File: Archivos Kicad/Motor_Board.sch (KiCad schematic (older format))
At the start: 56 parts, among them IC1 L298, P1 CONN_2_V, P2 CONN_2_V, P3 CONN_2_V, SW1 SWITCH_INV, U1 74HC04, U2 7805

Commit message: Modificaciones: Se eliminaron los HC04 y se habilitaron directamente las entradas (IN1, IN2, IN3, IN4). Las salidas de los motores se conectaron directamente al L298.
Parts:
- removed U1: 74HC04, symbol 74HC04
- added D20, D21: Led_Small, symbol Led_Small
- added OK5, OK6: 4N35, DIL06, symbol 4N35
- added R16, R17: 330, symbol R
- added R18, R19: 1K, symbol R
- R11, R13, R14: value R -> 1K; Digikey# (none) -> Value; LibPart (none) -> Value; Manf (none) -> Value; Manf# (none) -> Value
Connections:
- net labels added: GPIO3, GPIO5
- wire segments 181 -> 199
- no-connect marks 29 -> 25
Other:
- moved on the sheet: D10, D11, D12, D13, D14, D15, D16, D17, D18, D5, D6, D9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

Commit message: Modificaciones en la asignación de tierras entre los optoacopladores y el conector de la Edu Ciaa. Nueva conexión de la tierra del led D19.
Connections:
- net labels removed: GND
- wire segments 199 -> 191
- no-connect marks 25 -> 34
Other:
- moved on the sheet: D1, D10, D11, D12, D13, D14, D15, D16, D17, D18, D2, D20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

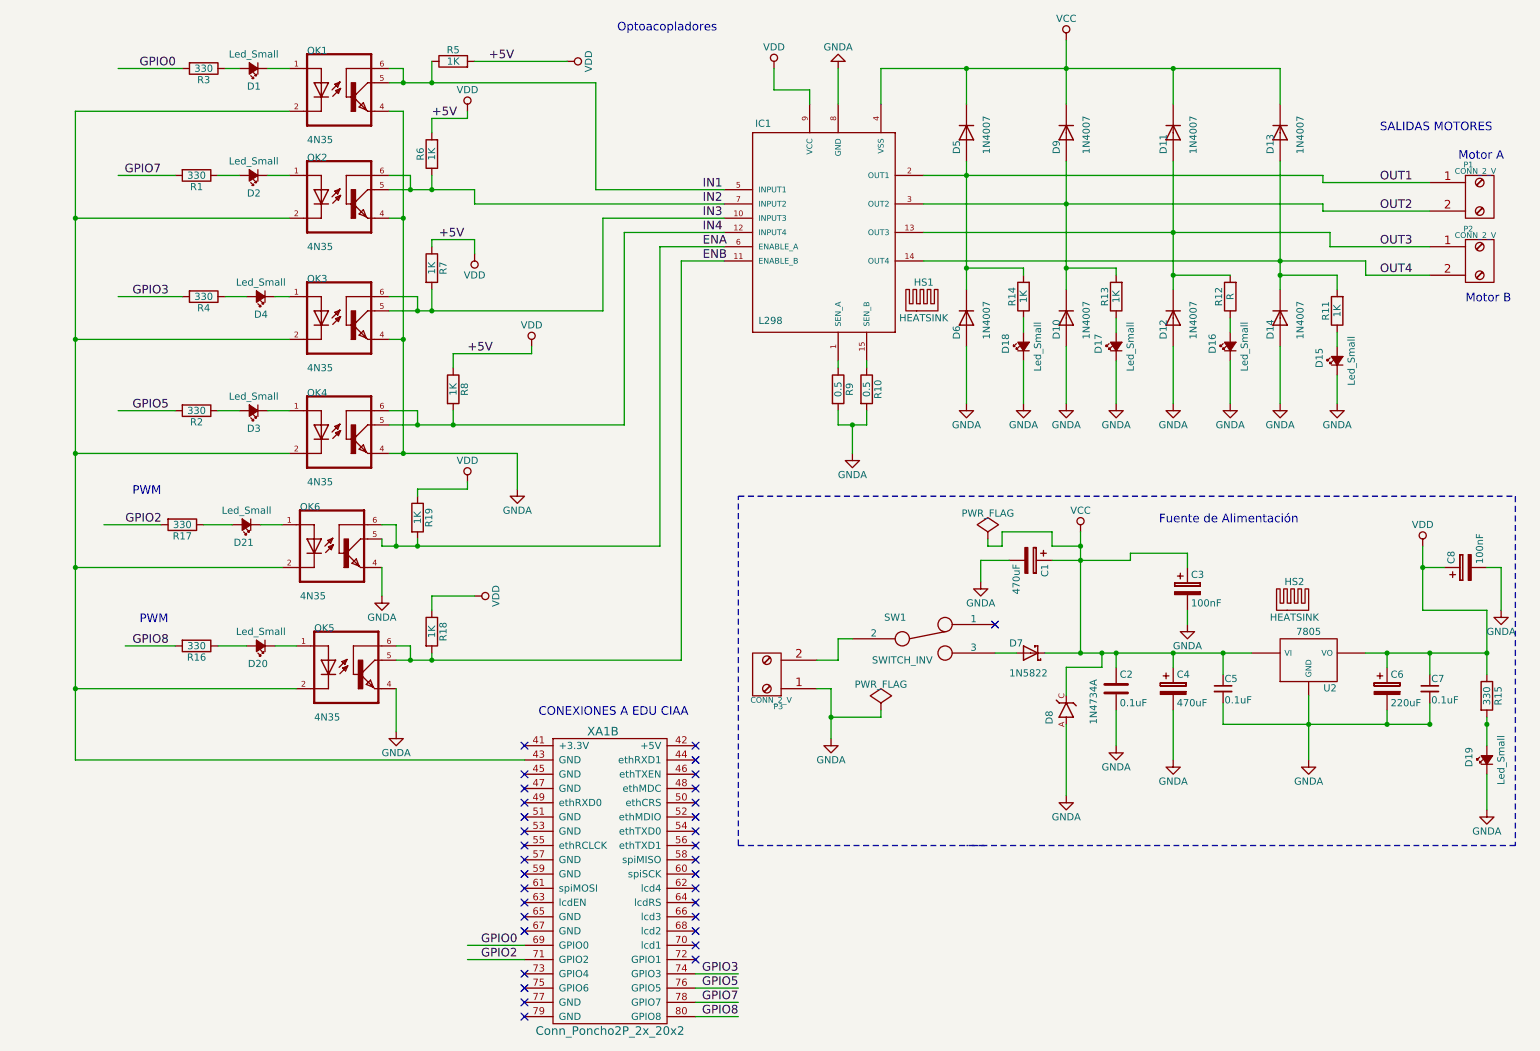
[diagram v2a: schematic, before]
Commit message: Modificación de los capacitores de desacople del L298.
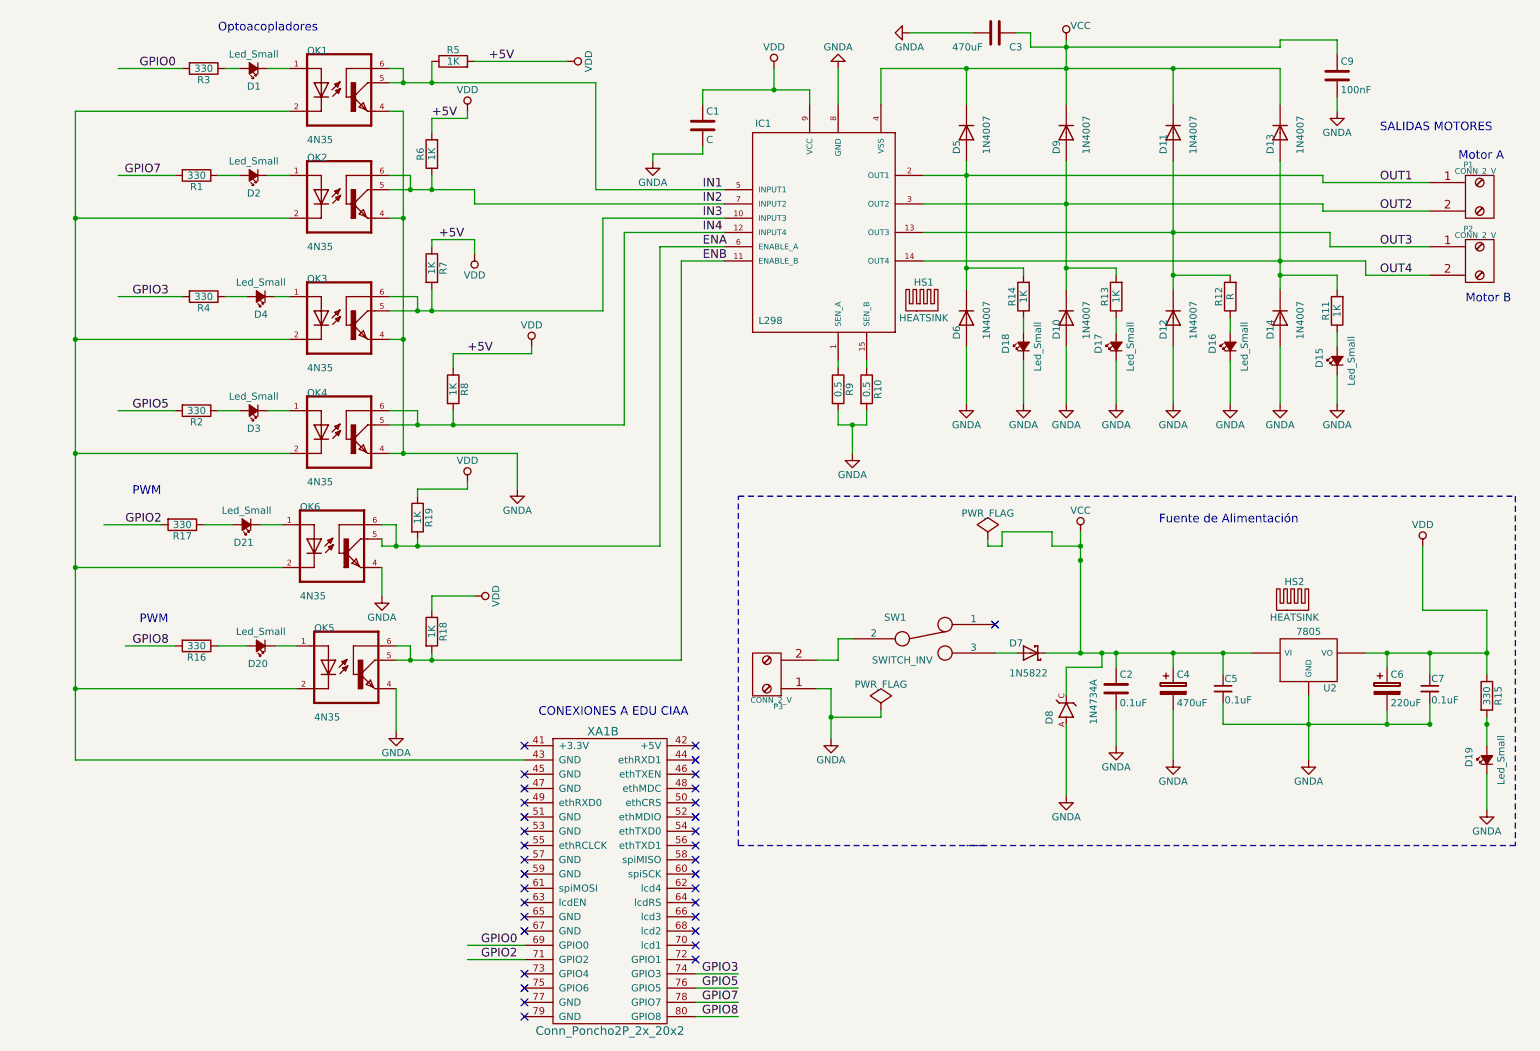
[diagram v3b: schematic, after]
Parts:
- removed C1: 470uF, symbol CP
- removed C3, C8: 100nF, symbol CP
- added C1: C, symbol C
- added C3: 470uF, symbol C
- added C9: 100nF, symbol C
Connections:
- wire segments 191 -> 193
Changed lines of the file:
@@
-$EndComp
-$Comp
-L CP C3
-U 1 1 5796EB2B
-P 8800 4500
-F 0 "C3" H 8825 4600 50  0000 L CNN
-F 1 "100nF" H 8825 4400 50  0000 L CNN
-F 2 "" H 8838 4350 50  0000 C CNN
-F 3 "" H 8800 4500 50  0000 C CNN
-F 4 "Value" H 8800 4500 60  0001 C CNN "Digikey#"
-F 5 "Value" H 8800 4500 60  0001 C CNN "LibPart"
-F 6 "Value" H 8800 4500 60  0001 C CNN "Manf"
-F 7 "Value" H 8800 4500 60  0001 C CNN "Manf#"
-	1    8800 4500
-	1    0    0    -1
-$EndComp
-$Comp
-L CP C1
-U 1 1 5796F04C
-P 7700 4300
-F 0 "C1" H 7725 4400 50  0000 L CNN
-F 1 "470uF" H 7725 4200 50  0000 L CNN
-F 2 "" H 7738 4150 50  0000 C CNN
-F 3 "" H 7700 4300 50  0000 C CNN
-F 4 "Value" H 7700 4300 60  0001 C CNN "Digikey#"
-F 5 "Value" H 7700 4300 60  0001 C CNN "LibPart"
-F 6 "Value" H 7700 4300 60  0001 C CNN "Manf"
-F 7 "Value" H 7700 4300 60  0001 C CNN "Manf#"
-	1    7700 4300
-	0    1    1    0
-$EndComp
-$Comp
-L CP C8
-U 1 1 57972ECB
-P 10750 4350
-F 0 "C8" H 10775 4450 50  0000 L CNN
-F 1 "100nF" H 10775 4250 50  0000 L CNN
-F 2 "" H 10788 4200 50  0000 C CNN
-F 3 "" H 10750 4350 50  0000 C CNN
-F 4 "Value" H 10750 4350 60  0001 C CNN "Digikey#"
-F 5 "Value" H 10750 4350 60  0001 C CNN "LibPart"
-F 6 "Value" H 10750 4350 60  0001 C CNN "Manf"
-F 7 "Value" H 10750 4350 60  0001 C CNN "Manf#"
-	1    10750 4350
-	0    -1   -1   0
 $EndComp
 $Comp
@@
 	1    0    0    -1
 $EndComp
-Text Notes 4800 600  0    60   ~ 0
+Text Notes 2000 600  0    60   ~ 0
 Optoacopladores
 Text Label 3750 2850 0    60   ~ 0
@@
 P 7950 650
 F 0 "#PWR05" H 7950 500 50  0001 C CNN
-F 1 "VCC" H 7950 800 50  0000 C CNN
+F 1 "VCC" H 8050 750 50  0000 C CNN
 F 2 "" H 7950 650 50  0000 C CNN
 F 3 "" H 7950 650 50  0000 C CNN
@@
 L GNDA #PWR06
 U 1 1 5798E1A8
-P 7350 4450
-F 0 "#PWR06" H 7350 4200 50  0001 C CNN
-F 1 "GNDA" H 7350 4300 50  0000 C CNN
-F 2 "" H 7350 4450 50  0000 C CNN
-F 3 "" H 7350 4450 50  0000 C CNN
-	1    7350 4450
-	1    0    0    -1
+P 6850 600
+F 0 "#PWR06" H 6850 350 50  0001 C CNN
+F 1 "GNDA" V 6950 600 50  0000 C CNN
+F 2 "" H 6850 600 50  0000 C CNN
+F 3 "" H 6850 600 50  0000 C CNN
+	1    6850 600
+	0    1    1    0
 $EndComp
 NoConn ~ 5350 5600
@@
 $Comp
 L GNDA #PWR015
-U 1 1 579937D2
-P 11000 4650
-F 0 "#PWR015" H 11000 4400 50  0001 C CNN
-F 1 "GNDA" H 11000 4500 50  0000 C CNN
-F 2 "" H 11000 4650 50  0000 C CNN
-F 3 "" H 11000 4650 50  0000 C CNN
-	1    11000 4650
-	1    0    0    -1
-$EndComp
-$Comp
-L GNDA #PWR016
 U 1 1 57995F21
 P 6450 3550
-F 0 "#PWR016" H 6450 3300 50  0001 C CNN
+F 0 "#PWR015" H 6450 3300 50  0001 C CNN
 F 1 "GNDA" H 6450 3400 50  0000 C CNN
 F 2 "" H 6450 3550 50  0000 C CNN
@@
 $EndComp
 $Comp
-L GNDA #PWR017
+L GNDA #PWR016
 U 1 1 57998542
 P 7250 3200
-F 0 "#PWR017" H 7250 2950 50  0001 C CNN
+F 0 "#PWR016" H 7250 2950 50  0001 C CNN
 F 1 "GNDA" H 7250 3050 50  0000 C CNN
 F 2 "" H 7250 3200 50  0000 C CNN
@@
 $EndComp
 $Comp
-L GNDA #PWR018
+L GNDA #PWR017
 U 1 1 5799B580
 P 7950 5950
-F 0 "#PWR018" H 7950 5700 50  0001 C CNN
+F 0 "#PWR017" H 7950 5700 50  0001 C CNN
 F 1 "GNDA" H 7950 5800 50  0000 C CNN
 F 2 "" H 7950 5950 50  0000 C CNN
@@
 $EndComp
 $Comp
+L GNDA #PWR018
+U 1 1 5799BB75
+P 9850 1150
+F 0 "#PWR018" H 9850 900 50  0001 C CNN
+F 1 "GNDA" H 9850 1000 50  0000 C CNN
+F 2 "" H 9850 1150 50  0000 C CNN
+F 3 "" H 9850 1150 50  0000 C CNN
+	1    9850 1150
+	1    0    0    -1
+$EndComp
+$Comp
 L GNDA #PWR019
-U 1 1 5799BB75
-P 8800 4750
-F 0 "#PWR019" H 8800 4500 50  0001 C CNN
-F 1 "GNDA" H 8800 4600 50  0000 C CNN
-F 2 "" H 8800 4750 50  0000 C CNN
-F 3 "" H 8800 4750 50  0000 C CNN
-	1    8800 4750
-	1    0    0    -1
-$EndComp
-$Comp
-L GNDA #PWR020
 U 1 1 5799C1B7
 P 6350 850
-F 0 "#PWR020" H 6350 600 50  0001 C CNN
+F 0 "#PWR019" H 6350 600 50  0001 C CNN
 F 1 "GNDA" H 6350 700 50  0000 C CNN
 F 2 "" H 6350 850 50  0000 C CNN
@@
 $EndComp
 $Comp
-L PWR_FLAG #FLG021
+L PWR_FLAG #FLG020
 U 1 1 5799CDEB
 P 6650 5350
-F 0 "#FLG021" H 6650 5445 50  0001 C CNN
+F 0 "#FLG020" H 6650 5445 50  0001 C CNN
 F 1 "PWR_FLAG" H 6650 5530 50  0000 C CNN
 F 2 "" H 6650 5350 50  0000 C CNN
@@
 $EndComp
 $Comp
-L GNDA #PWR022
+L GNDA #PWR021
 U 1 1 579AB5D5
 P 7650 3200
-F 0 "#PWR022" H 7650 2950 50  0001 C CNN
+F 0 "#PWR021" H 7650 2950 50  0001 C CNN
 F 1 "GNDA" H 7650 3050 50  0000 C CNN
 F 2 "" H 7650 3200 50  0000 C CNN
@@
 $EndComp
 $Comp
-L GNDA #PWR023
+L GNDA #PWR022
 U 1 1 579AB65B
 P 7950 3200
-F 0 "#PWR023" H 7950 2950 50  0001 C CNN
+F 0 "#PWR022" H 7950 2950 50  0001 C CNN
 F 1 "GNDA" H 7950 3050 50  0000 C CNN
 F 2 "" H 7950 3200 50  0000 C CNN
@@
 $EndComp
 $Comp
-L GNDA #PWR024
+L GNDA #PWR023
 U 1 1 579AB6E1
 P 8300 3200
-F 0 "#PWR024" H 8300 2950 50  0001 C CNN
+F 0 "#PWR023" H 8300 2950 50  0001 C CNN
 F 1 "GNDA" H 8300 3050 50  0000 C CNN
 F 2 "" H 8300 3200 50  0000 C CNN
@@
 $EndComp
 $Comp
-L GNDA #PWR025
+L GNDA #PWR024
 U 1 1 579AB7D9
 P 8700 3200
-F 0 "#PWR025" H 8700 2950 50  0001 C CNN
+F 0 "#PWR024" H 8700 2950 50  0001 C CNN
 F 1 "GNDA" H 8700 3050 50  0000 C CNN
 F 2 "" H 8700 3200 50  0000 C CNN
@@
 $EndComp
 $Comp
-L GNDA #PWR026
+L GNDA #PWR025
 U 1 1 579AB85F
 P 9100 3200
-F 0 "#PWR026" H 9100 2950 50  0001 C CNN
+F 0 "#PWR025" H 9100 2950 50  0001 C CNN
 F 1 "GNDA" H 9100 3050 50  0000 C CNN
 F 2 "" H 9100 3200 50  0000 C CNN
@@
 $EndComp
 $Comp
-L GNDA #PWR027
+L GNDA #PWR026
 U 1 1 579AB8E5
 P 9450 3200
-F 0 "#PWR027" H 9450 2950 50  0001 C CNN
+F 0 "#PWR026" H 9450 2950 50  0001 C CNN
 F 1 "GNDA" H 9450 3050 50  0000 C CNN
 F 2 "" H 9450 3200 50  0000 C CNN
@@
 $EndComp
 $Comp
-L GNDA #PWR028
+L GNDA #PWR027
 U 1 1 579AD1DA
 P 9850 3200
-F 0 "#PWR028" H 9850 2950 50  0001 C CNN
+F 0 "#PWR027" H 9850 2950 50  0001 C CNN
 F 1 "GNDA" H 9850 3050 50  0000 C CNN
 F 2 "" H 9850 3200 50  0000 C CNN
@@
 $EndComp
 $Comp
-L GNDA #PWR029
+L GNDA #PWR028
 U 1 1 579B03A9
 P 4100 3800
-F 0 "#PWR029" H 4100 3550 50  0001 C CNN
+F 0 "#PWR028" H 4100 3550 50  0001 C CNN
 F 1 "GNDA" H 4100 3650 50  0000 C CNN
 F 2 "" H 4100 3800 50  0000 C CNN
@@
 $EndComp
 $Comp
-L GNDA #PWR030
+L GNDA #PWR029
 U 1 1 579B552D
 P 3250 5500
-F 0 "#PWR030" H 3250 5250 50  0001 C CNN
+F 0 "#PWR029" H 3250 5250 50  0001 C CNN
 F 1 "GNDA" H 3250 5350 50  0000 C CNN
 F 2 "" H 3250 5500 50  0000 C CNN
@@
 $EndComp
 $Comp
-L GNDA #PWR031
+L GNDA #PWR030
 U 1 1 579B5C0D
 P 3150 4550
-F 0 "#PWR031" H 3150 4300 50  0001 C CNN
+F 0 "#PWR030" H 3150 4300 50  0001 C CNN
 F 1 "GNDA" H 3150 4400 50  0000 C CNN
 F 2 "" H 3150 4550 50  0000 C CNN
@@
 $EndComp
 $Comp
-L VDD #PWR032
+L VDD #PWR031
 U 1 1 579B7432
 P 3750 3750
-F 0 "#PWR032" H 3750 3600 50  0001 C CNN
+F 0 "#PWR031" H 3750 3600 50  0001 C CNN
 F 1 "VDD" H 3750 3900 50  0000 C CNN
 F 2 "" H 3750 3750 50  0000 C CNN
@@
 $EndComp
 $Comp
-L VDD #PWR033
+L VDD #PWR032
 U 1 1 579BBC29
 P 3800 4550
-F 0 "#PWR033" H 3800 4400 50  0001 C CNN
+F 0 "#PWR032" H 3800 4400 50  0001 C CNN
 F 1 "VDD" H 3800 4700 50  0000 C CNN
 F 2 "" H 3800 4550 50  0000 C CNN
@@
 Connection ~ 8050 4950
 Wire Wire Line
-	7850 4300 8400 4300
-Wire Wire Line
-	8800 4250 8800 4350
+	7700 700  9450 700
+Wire Wire Line
+	9850 650  9850 750
 Connection ~ 8050 4300
 Wire Wire Line
-	8800 4650 8800 4750
+	9850 1050 9850 1150
 Connection ~ 10900 4950
 Wire Wire Line
@@
 Wire Wire Line
 	10450 4650 10900 4650
-Wire Wire Line
-	10600 4350 10450 4350
-Connection ~ 10450 4350
-Wire Wire Line
-	10900 4350 11000 4350
-Wire Wire Line
-	11000 4350 11000 4650
 Wire Wire Line
 	7600 4950 7450 4950
@@
 Connection ~ 3500 950
 Wire Wire Line
-	8400 4300 8400 4250
-Wire Wire Line
-	8400 4250 8800 4250
-Wire Wire Line
-	6150 1100 6150 1000
-Wire Wire Line
-	6150 1000 5900 1000
+	9450 700  9450 650
+Wire Wire Line
+	9450 650  9850 650
+Wire Wire Line
+	6150 1000 6150 1100
+Wire Wire Line
+	5400 1000 6150 1000
 Wire Wire Line
 	10050 4950 10900 4950
@@
 	3650 2850 4200 2850
 Wire Wire Line
-	7350 4450 7350 4300
-Wire Wire Line
-	7350 4300 7550 4300
+	6850 600  7300 600
 Wire Wire Line
 	3750 1200 3750 1150
@@
 NoConn ~ 4150 7500
 $Comp
-L PWR_FLAG #FLG034
+L PWR_FLAG #FLG033
 U 1 1 579B8264
 P 7400 4150
-F 0 "#FLG034" H 7400 4245 50  0001 C CNN
+F 0 "#FLG033" H 7400 4245 50  0001 C CNN
 F 1 "PWR_FLAG" H 7400 4330 50  0000 C CNN
 F 2 "" H 7400 4150 50  0000 C CNN
@@
 	7400 4200 7400 4150
 Connection ~ 8050 4200
+Connection ~ 7950 700
+$Comp
+L C C9
+U 1 1 579C259C
+P 9850 900
+F 0 "C9" H 9875 1000 50  0000 L CNN
+F 1 "100nF" H 9875 800 50  0000 L CNN
+F 2 "" H 9888 750 50  0000 C CNN
+F 3 "" H 9850 900 50  0000 C CNN
+F 4 "Value" H 9850 900 60  0001 C CNN "Digikey#"
+F 5 "Value" H 9850 900 60  0001 C CNN "LibPart"
+F 6 "Value" H 9850 900 60  0001 C CNN "Manf"
+F 7 "Value" H 9850 900 60  0001 C CNN "Manf#"
+	1    9850 900
+	1    0    0    -1
+$EndComp
+$Comp
+L C C3
+U 1 1 579C2C83
+P 7450 600
+F 0 "C3" V 7550 700 50  0000 L CNN
+F 1 "470uF" V 7550 300 50  0000 L CNN
+F 2 "" H 7488 450 50  0000 C CNN
+F 3 "" H 7450 600 50  0000 C CNN
+F 4 "Value" H 7450 600 60  0001 C CNN "Digikey#"
+F 5 "Value" H 7450 600 60  0001 C CNN "LibPart"
+F 6 "Value" H 7450 600 60  0001 C CNN "Manf"
+F 7 "Value" H 7450 600 60  0001 C CNN "Manf#"
+	1    7450 600
+	0    1    1    0
+$EndComp
+Wire Wire Line
+	7600 600  7700 600
+Wire Wire Line
+	7700 600  7700 700
+$Comp
+L C C1
+U 1 1 579C3660
+P 5400 1250
+F 0 "C1" H 5425 1350 50  0000 L CNN
+F 1 "C" H 5425 1150 50  0000 L CNN
+F 2 "" H 5438 1100 50  0000 C CNN
+F 3 "" H 5400 1250 50  0000 C CNN
+	1    5400 1250
+	1    0    0    -1
+$EndComp
+Wire Wire Line
+	5400 1000 5400 1100
+Connection ~ 5900 1000
+$Comp
+L GNDA #PWR034
+U 1 1 579C38E8
+P 5050 1500
+F 0 "#PWR034" H 5050 1250 50  0001 C CNN
+F 1 "GNDA" H 5050 1350 50  0000 C CNN
+F 2 "" H 5050 1500 50  0000 C CNN
+F 3 "" H 5050 1500 50  0000 C CNN
+	1    5050 1500
+	1    0    0    -1
+$EndComp
+Wire Wire Line
+	5050 1500 5050 1450
+Wire Wire Line
+	5050 1450 5400 1450
+Wire Wire Line
+	5400 1450 5400 1400
 $EndSCHEMATC
